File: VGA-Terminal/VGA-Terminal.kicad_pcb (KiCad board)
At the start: 2 copper layers, 51 x 44 mm, 7 parts, among them J1 DB15_Female_HighDensity_Mount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, J2 Hotend, J3 X-Endstop, Fan, Custom, J4 Fan & Custom

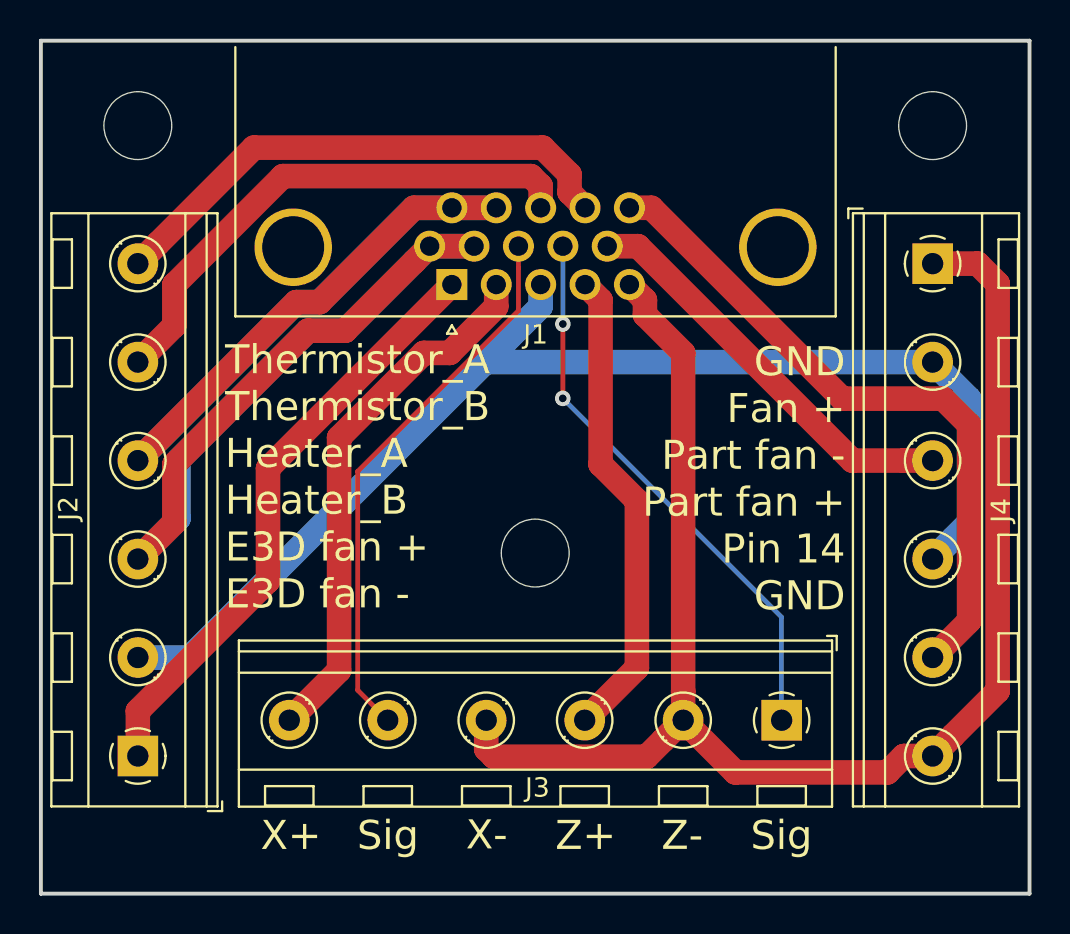
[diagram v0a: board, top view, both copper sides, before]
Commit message: Corrected the footprint
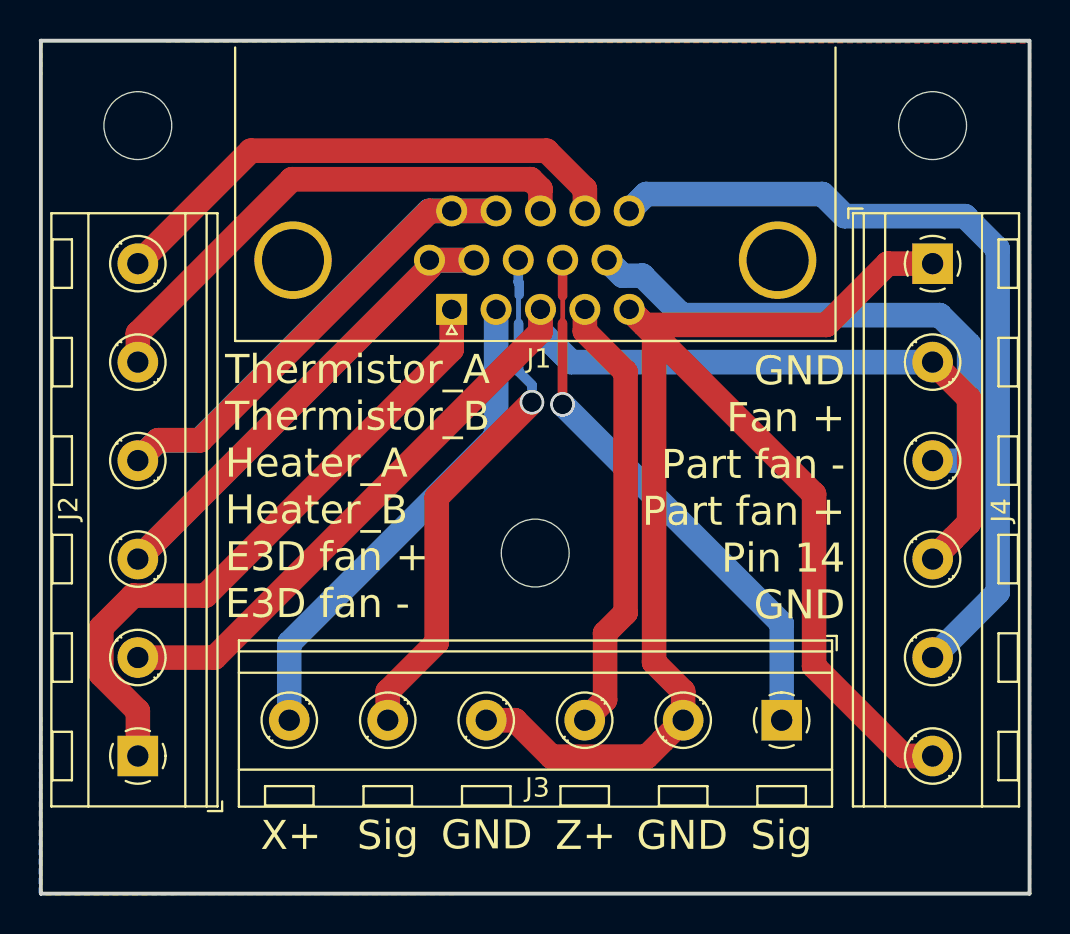
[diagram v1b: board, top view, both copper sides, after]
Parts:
- J1: footprint Connectors_OWN:DSUB-15-HD_Female_Horizontal_P2.29x1.98mm_EdgePinOffset8.35mm_Housed_MountingHolesOffset10.89mm -> Connectors_OWN:DSUB-15-HD_Assmann
- moved J1 23.5 mm to (128.9, 61.9)
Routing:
- net Pin14: track 35.0 -> 43.0 mm
- net Part_N: track 21.4 -> 28.1 mm
- net HOT_B: track 51.6 -> 47.9 mm
- net V_FAN: track 66.1 -> 62.6 mm
- net E3D_N: track 31.0 -> 33.5 mm
- net Vcc_X: track 27.7 -> 25.6 mm
- net Vcc_Z: track 24.7 -> 22.9 mm
- net X_Sig: track 28.5 -> 27.1 mm, vias 0 -> 1
- net Z_Sig: track 29.1 -> 28.4 mm, vias 2 -> 1
- net GND: track 80.1 -> 80.6 mm
- added copper zone on B.Cu, net GND
- added copper zone on F.Cu, net GND
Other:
- board text added: "GND"
- board text added: "HEVO Hotend VGA Breakout by Thorsten Reichelt"
- board text added: "v0.3 / 2019-02-11"
- board text removed: "X-"
- board text removed: "Z-"

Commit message: Added these....
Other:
- board text added: "HEVO X-Carriage VGA Breakout by Thorsten Reichelt"
- board text removed: "HEVO Hotend VGA Breakout by Thorsten Reichelt"
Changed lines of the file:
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@@
     (effects (font (size 1.5 1.5) (thickness 0.3)) (justify mirror))
   )
-  (gr_text "HEVO Hotend VGA Breakout\nby Thorsten Reichelt" (at 113.01 65.39) (layer B.SilkS)
+  (gr_text "HEVO X-Carriage VGA Breakout\nby Thorsten Reichelt" (at 113.4 65.35) (layer B.SilkS)
     (effects (font (size 1.5 1.5) (thickness 0.3)) (justify mirror))
   )
